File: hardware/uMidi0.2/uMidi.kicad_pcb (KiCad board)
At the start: 2 copper layers, 71.1 x 43.2 mm, 43 parts, among them CON1 USB-MINI-B, IC1 6N138, IC2 ATXMEGA128A4U-M, P1 MIDI In, P2 MIDI Thru, P3 MIDI T/O, P4 MIDI Out, P5 5..12 V, P6 PDI, P7 GPIO1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

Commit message: Move jumper to top layer
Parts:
- JP1: moved to F.Cu
- moved JP1 0.89 mm to (93.6, 154.9)
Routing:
- net Net-(C12-Pad1): track 27.3 -> 8.75 mm
- net TXD: track 30.4 -> 29.1 mm, vias 2 -> 0
- net RXD: track 3.82 -> 4.70 mm, vias 1 -> 0
- net Net-(JP1-Pad2): track 3.30 -> 4.19 mm, vias 1 -> 0
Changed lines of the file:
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@@
     (links 120)
     (no_connects 46)
-    (area 64.280952 119.12205 143.873784 167.80905)
+    (area 67.259999 121.869999 138.480001 165.150001)
     (thickness 1.6)
     (drawings 4)
-    (tracks 268)
+    (tracks 257)
     (zones 0)
     (modules 43)
@@
     (pad_to_mask_clearance 0)
     (aux_axis_origin 0 0)
-    (visible_elements FFFFFF3F)
+    (visible_elements FFFFFF1F)
     (pcbplotparams
       (layerselection 0x00030_80000001)
@@
       (net 2 GND))
   )
-  (module Solderjumper:SJ3 placed (layer B.Cu)
-    (at 92.71 154.94 270)
-    (fp_text reference JP1 (at 0 2.54 270) (layer B.SilkS)
-      (effects (font (size 1.5 1.5) (thickness 0.15)) (justify mirror))
-    )
-    (fp_text value JUMPER3 (at 0 -2.54 270) (layer B.SilkS)
-      (effects (font (size 1.5 1.5) (thickness 0.15)) (justify mirror))
-    )
-    (pad 2 smd rect (at 0 0 270) (size 1 1) (layers B.Cu B.Paste B.Mask)
+  (module Solderjumper:SJ3 placed (layer F.Cu)
+    (at 93.599 154.94 270)
+    (fp_text reference JP1 (at 0 -2.54 270) (layer F.SilkS)
+      (effects (font (size 1.5 1.5) (thickness 0.15)))
+    )
+    (fp_text value JUMPER3 (at 0 2.54 270) (layer F.SilkS)
+      (effects (font (size 1.5 1.5) (thickness 0.15)))
+    )
+    (pad 2 smd rect (at 0 0 270) (size 1 1) (layers F.Cu F.Paste F.Mask)
       (net 47 "Net-(JP1-Pad2)"))
-    (pad 1 smd rect (at -1.3 0 270) (size 1 1) (layers B.Cu B.Paste B.Mask)
+    (pad 1 smd rect (at -1.3 0 270) (size 1 1) (layers F.Cu F.Paste F.Mask)
       (net 13 RXD))
-    (pad 3 smd rect (at 1.3 0 270) (size 1 1) (layers B.Cu B.Paste B.Mask)
+    (pad 3 smd rect (at 1.3 0 270) (size 1 1) (layers F.Cu F.Paste F.Mask)
       (net 37 TXD))
   )
@@
   (segment (start 118.05158 150.80742) (end 118.05158 149.86) (width 0.3) (layer F.Cu) (net 4))
   (segment (start 115.443 151.384) (end 115.57 151.257) (width 0.15) (layer F.Cu) (net 4))
+  (segment (start 107.442 145.542) (end 110.109 145.542) (width 0.3) (layer F.Cu) (net 5))
   (segment (start 122.61 142.01) (end 123.293 142.01) (width 0.3) (layer F.Cu) (net 5))
   (segment (start 123.63958 141.66342) (end 124.206 141.66342) (width 0.3) (layer F.Cu) (net 5))
   (segment (start 123.293 142.01) (end 123.63958 141.66342) (width 0.3) (layer F.Cu) (net 5))
-  (segment (start 97.79 158.75) (end 97.79 152.908) (width 0.3) (layer F.Cu) (net 5))
-  (segment (start 105.156 145.542) (end 110.109 145.542) (width 0.3) (layer F.Cu) (net 5))
-  (segment (start 97.79 152.908) (end 105.156 145.542) (width 0.3) (layer F.Cu) (net 5))
   (segment (start 110.109 145.542) (end 111.76 145.542) (width 0.3) (layer F.Cu) (net 5))
   (segment (start 111.76 145.542) (end 111.76 145.22958) (width 0.3) (layer F.Cu) (net 5))
@@
   (segment (start 78.74 137.795) (end 78.74 139.70508) (width 0.15) (layer F.Cu) (net 12))
   (segment (start 78.105 137.16) (end 78.74 137.795) (width 0.15) (layer F.Cu) (net 12))
-  (segment (start 89.408 152.4) (end 90.17 152.4) (width 0.15) (layer F.Cu) (net 13))
-  (segment (start 91.41 153.64) (end 92.71 153.64) (width 0.15) (layer B.Cu) (net 13))
-  (segment (start 90.805 153.035) (end 91.41 153.64) (width 0.15) (layer B.Cu) (net 13))
-  (via (at 90.805 153.035) (size 0.6) (layers F.Cu B.Cu) (net 13))
-  (segment (start 90.17 152.4) (end 90.805 153.035) (width 0.15) (layer F.Cu) (net 13))
+  (segment (start 89.408 152.4) (end 90.551 152.4) (width 0.15) (layer F.Cu) (net 13))
+  (segment (start 91.791 153.64) (end 93.599 153.64) (width 0.15) (layer F.Cu) (net 13))
+  (segment (start 90.551 152.4) (end 91.791 153.64) (width 0.15) (layer F.Cu) (net 13))
   (segment (start 122.61 146.01) (end 122.61 153.361) (width 0.15) (layer F.Cu) (net 14))
   (segment (start 118.11 160.02) (end 119.38 161.29) (width 0.15) (layer F.Cu) (net 14))
@@
   (segment (start 113.03 127) (end 111.76 125.73) (width 0.15) (layer F.Cu) (net 32))
   (segment (start 113.03 140.43) (end 113.03 127) (width 0.15) (layer F.Cu) (net 32))
-  (segment (start 113.61 146.01) (end 113.451 146.01) (width 0.15) (layer F.Cu) (net 37) (status C00000))
-  (segment (start 113.451 146.01) (end 112.268 147.193) (width 0.15) (layer F.Cu) (net 37) (status 400000))
-  (segment (start 112.268 147.193) (end 104.902 147.193) (width 0.15) (layer F.Cu) (net 37))
-  (segment (start 104.902 147.193) (end 98.425 153.67) (width 0.15) (layer F.Cu) (net 37))
-  (segment (start 98.425 153.67) (end 98.425 156.083) (width 0.15) (layer F.Cu) (net 37))
-  (via (at 98.425 156.083) (size 0.6) (layers F.Cu B.Cu) (net 37))
-  (segment (start 98.425 156.083) (end 98.268 156.24) (width 0.15) (layer B.Cu) (net 37))
-  (segment (start 98.268 156.24) (end 92.71 156.24) (width 0.15) (layer B.Cu) (net 37) (status 800000))
-  (segment (start 89.408 157.48) (end 90.17 157.48) (width 0.15) (layer F.Cu) (net 37))
-  (segment (start 91.41 156.24) (end 92.71 156.24) (width 0.15) (layer B.Cu) (net 37))
-  (segment (start 90.805 156.845) (end 91.41 156.24) (width 0.15) (layer B.Cu) (net 37))
-  (via (at 90.805 156.845) (size 0.6) (layers F.Cu B.Cu) (net 37))
-  (segment (start 90.17 157.48) (end 90.805 156.845) (width 0.15) (layer F.Cu) (net 37))
-  (segment (start 115.61 148.01) (end 105.99 148.01) (width 0.15) (layer F.Cu) (net 38) (status 400000))
-  (segment (start 99.06 160.02) (end 97.79 161.29) (width 0.15) (layer F.Cu) (net 38) (status 800000))
+  (segment (start 93.599 156.24) (end 96.617 156.24) (width 0.15) (layer F.Cu) (net 37) (status 400000))
+  (segment (start 112.3 147.32) (end 113.61 146.01) (width 0.15) (layer F.Cu) (net 37) (status 800000))
+  (segment (start 105.537 147.32) (end 112.3 147.32) (width 0.15) (layer F.Cu) (net 37))
+  (segment (start 96.617 156.24) (end 105.537 147.32) (width 0.15) (layer F.Cu) (net 37))
+  (segment (start 89.408 157.48) (end 90.805 157.48) (width 0.15) (layer F.Cu) (net 37))
+  (segment (start 92.045 156.24) (end 93.599 156.24) (width 0.15) (layer F.Cu) (net 37))
+  (segment (start 90.805 157.48) (end 92.045 156.24) (width 0.15) (layer F.Cu) (net 37))
+  (segment (start 113.61 146.01) (end 113.451 146.01) (width 0.15) (layer F.Cu) (net 37))
+  (segment (start 115.61 148.01) (end 105.99 148.01) (width 0.15) (layer F.Cu) (net 38))
+  (segment (start 99.06 160.02) (end 97.79 161.29) (width 0.15) (layer F.Cu) (net 38))
   (segment (start 99.06 154.94) (end 99.06 160.02) (width 0.15) (layer F.Cu) (net 38))
   (segment (start 105.99 148.01) (end 99.06 154.94) (width 0.15) (layer F.Cu) (net 38))
@@
   (segment (start 116.84 158.115) (end 120.61 154.345) (width 0.15) (layer F.Cu) (net 46))
   (segment (start 120.61 154.345) (end 120.61 148.01) (width 0.15) (layer F.Cu) (net 46))
-  (segment (start 89.408 154.94) (end 90.805 154.94) (width 0.15) (layer F.Cu) (net 47))
-  (segment (start 90.805 154.94) (end 92.71 154.94) (width 0.15) (layer B.Cu) (net 47))
-  (via (at 90.805 154.94) (size 0.6) (layers F.Cu B.Cu) (net 47))
+  (segment (start 89.408 154.94) (end 93.599 154.94) (width 0.15) (layer F.Cu) (net 47))
   (segment (start 71.12 137.16) (end 76.38542 137.16) (width 0.15) (layer F.Cu) (net 48))
   (segment (start 71.12 142.24) (end 73.025 142.24) (width 0.15) (layer F.Cu) (net 49))
@@
   (segment (start 86.995 158.75) (end 89.408 158.75) (width 0.15) (layer F.Cu) (net 63))
   (segment (start 84.455 156.21) (end 86.995 158.75) (width 0.15) (layer F.Cu) (net 63))
-  (segment (start 89.408 151.13) (end 91.75242 151.13) (width 0.3) (layer F.Cu) (net 64) (status C00000))
+  (segment (start 89.408 151.13) (end 91.75242 151.13) (width 0.3) (layer F.Cu) (net 64))
   (segment (start 93.472 135.89) (end 93.472 135.001) (width 0.3) (layer F.Cu) (net 64))
   (segment (start 92.47 133.999) (end 92.47 132.64) (width 0.3) (layer F.Cu) (net 64))

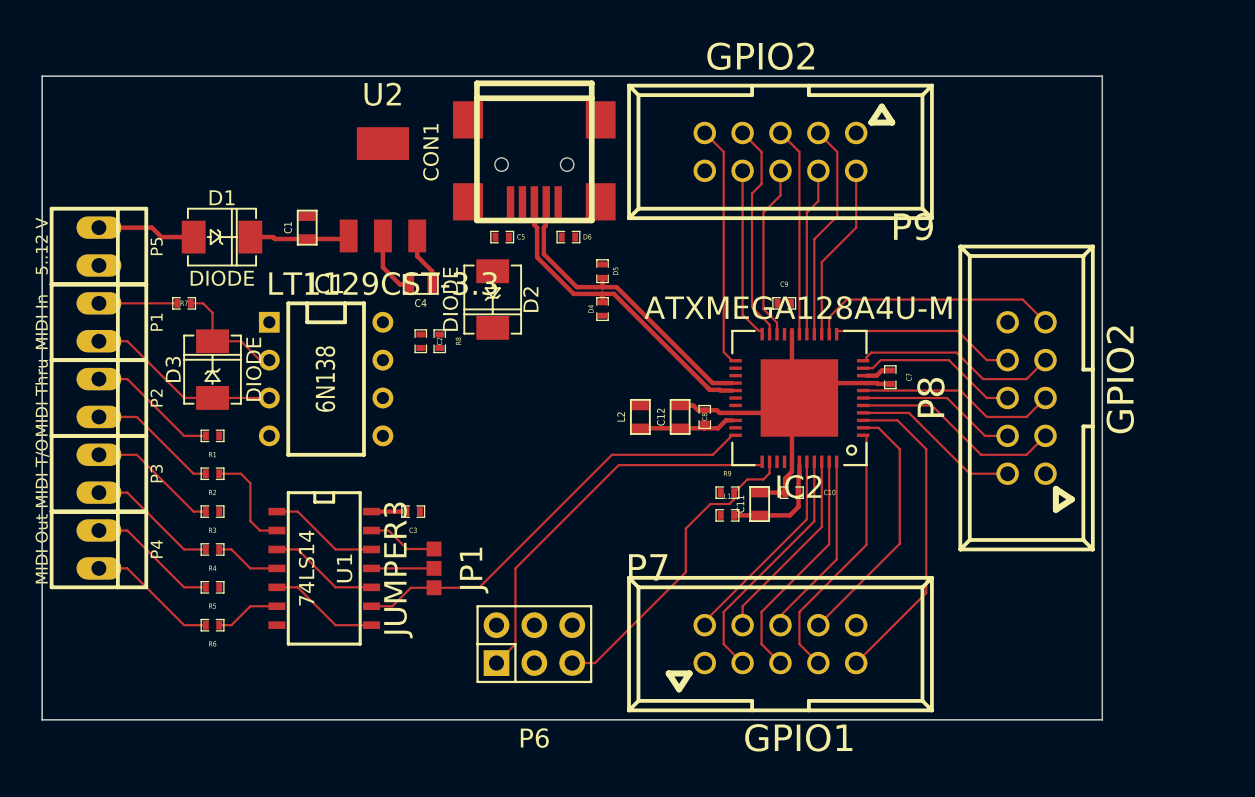
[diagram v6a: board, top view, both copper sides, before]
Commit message: Change all 0402 passives to 0603 packages
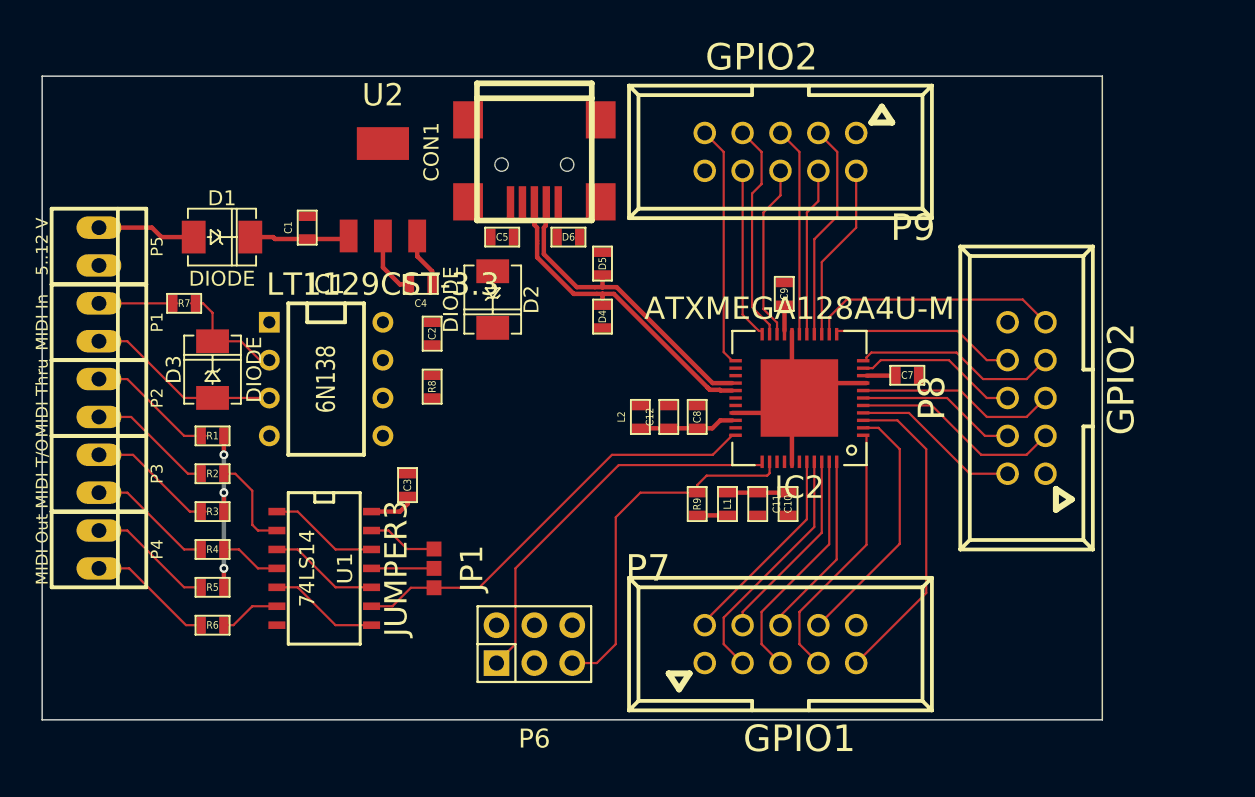
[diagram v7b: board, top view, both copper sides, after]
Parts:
- C10, C2, C3, C5, C7, C8, C9, D4, D5, D6, L1, R1, R2, R3, R4, R5, R6, R7, R8, R9: footprint SMD_Packages:SMD-0402 -> SMD_Packages:SMD-0603
- moved R8 3.09 mm to (93.5, 142.7)
- moved R9 2.17 mm to (111.3, 150.6), turned to 90 degrees
- moved C3 1.82 mm to (91.8, 149.4), turned to 90 degrees
- moved C7 1.15 mm to (125.3, 142.0), turned to 0 degrees
- moved C2 0.92 mm to (93.5, 139.2)
- moved C10 0.80 mm to (117.3, 150.6), turned to 270 degrees
- moved C12 0.76 mm to (109.3, 144.8)
- moved L1 0.76 mm to (113.3, 150.6), turned to 90 degrees
- moved C9 0.63 mm to (117.1, 136.5), turned to 90 degrees
- moved C8 0.51 mm to (111.3, 144.8)
- moved D4 0.51 mm to (104.9, 138.0)
- moved D5 0.51 mm to (104.9, 134.5)
- moved C11 0.13 mm to (115.3, 150.6), turned to 270 degrees
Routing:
- net VCC: track 6.01 -> 18.2 mm, vias 0 -> 3
- net GND: track 32.8 -> 23.6 mm
- net Net-(C10-Pad1): track 7.56 -> 4.06 mm
- net Net-(C12-Pad1): track 8.75 -> 12.1 mm
- net Net-(IC2-Pad35): track 21.0 -> 24.3 mm

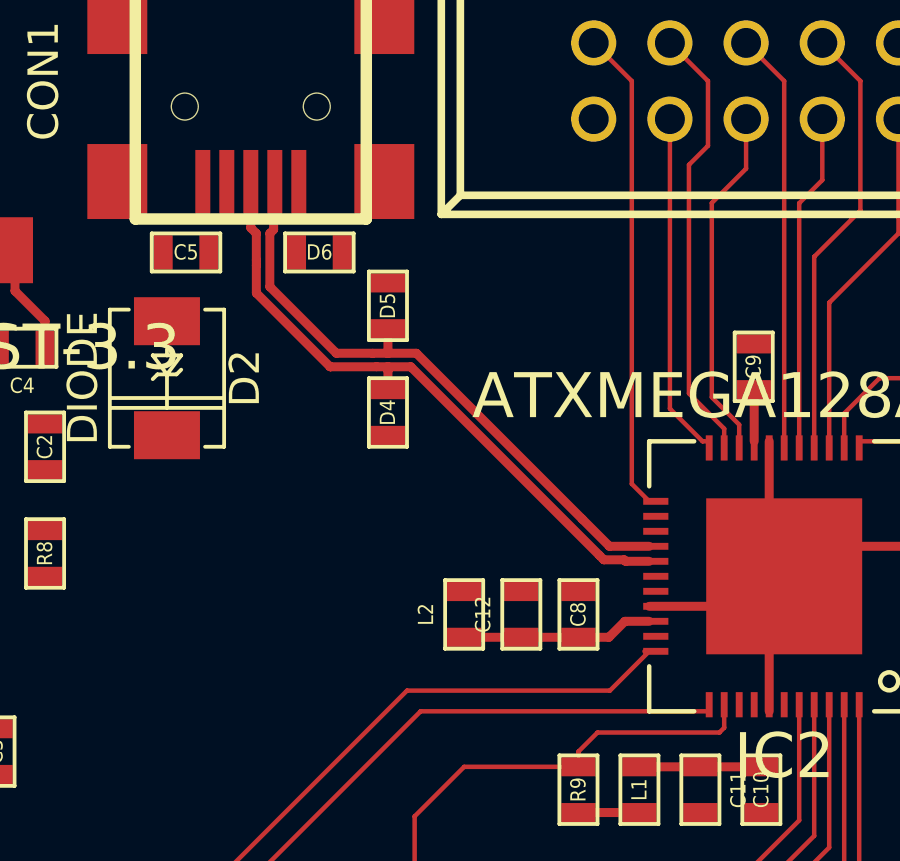
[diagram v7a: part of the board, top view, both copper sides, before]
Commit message: Optimize USB tracks
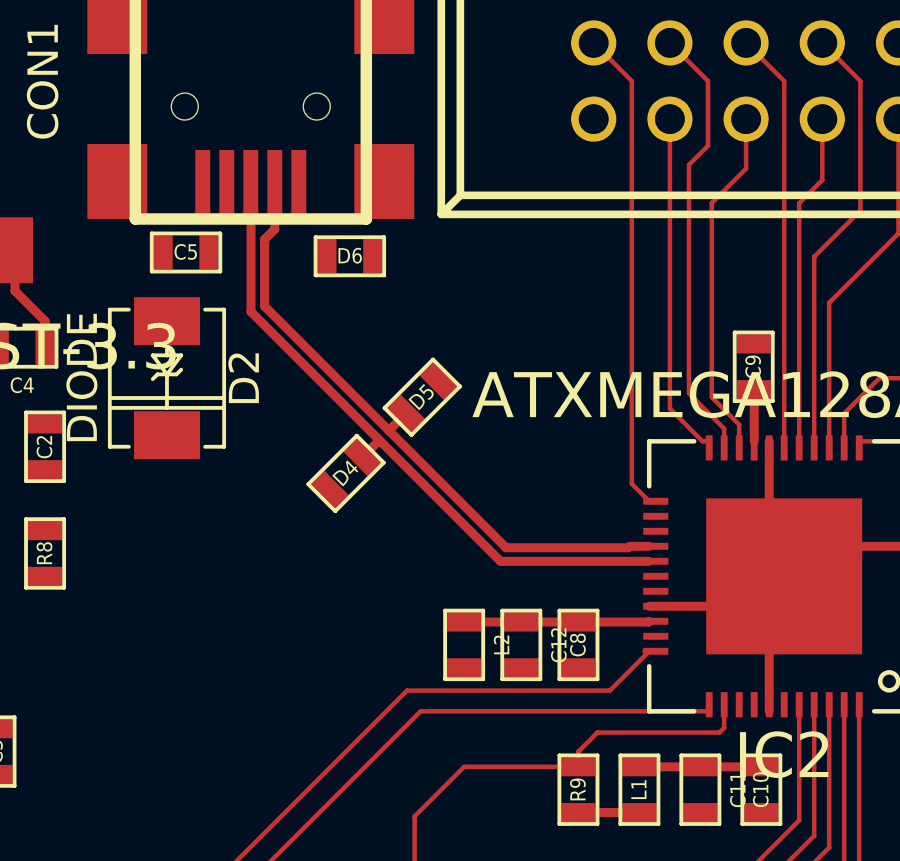
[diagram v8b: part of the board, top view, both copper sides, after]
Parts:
- moved D5 3.26 mm to (106.0, 137.5), turned to 225 degrees
- moved D4 2.47 mm to (103.5, 140.1), turned to 45 degrees
- moved D6 1.02 mm to (103.6, 132.8)
- moved C12 1.02 mm to (109.3, 145.8), turned to 270 degrees
- moved C8 1.02 mm to (111.3, 145.8), turned to 270 degrees
- moved L2 1.02 mm to (107.4, 145.8), turned to 90 degrees
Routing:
- net Net-(CON1-Pad2): track 20.4 -> 21.2 mm
